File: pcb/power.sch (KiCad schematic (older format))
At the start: 25 parts, among them U16 AP22811AW5-7‎, U17 TLV62585PDRLR, U18 LP5907MFX-3.3, U4 TLV62585PDRLR

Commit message: Switch to AP3441LSHE-7B in schematic
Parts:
- removed U17, U4: TLV62585PDRLR, launch:SOT-563, symbol launch:TLV62585DRLR
- added U17, U4: AP3441LSHE-7B, launch:W-DFN2020-8_Type_C, symbol launch:AP3441LSHE-7B
- C32, C34, C35, C48, C49, C50: value 10 uF -> 22 uF
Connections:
- wire segments 58 -> 60
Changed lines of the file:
@@
 L power:GND #PWR0248
 U 1 1 5F8E3978
-P 4500 4550
-F 0 "#PWR0248" H 4500 4300 50  0001 C CNN
-F 1 "GND" H 4505 4377 50  0000 C CNN
-F 2 "" H 4500 4550 50  0001 C CNN
-F 3 "" H 4500 4550 50  0001 C CNN
-	1    4500 4550
+P 4500 4600
+F 0 "#PWR0248" H 4500 4350 50  0001 C CNN
+F 1 "GND" H 4505 4427 50  0000 C CNN
+F 2 "" H 4500 4600 50  0001 C CNN
+F 3 "" H 4500 4600 50  0001 C CNN
+	1    4500 4600
 	1    0    0    -1
 $EndComp
@@
 	1    0    0    -1
 $EndComp
-$Comp
-L launch:TLV62585DRLR U17
-U 1 1 5F8E44C6
-P 4650 4250
-F 0 "U17" H 4975 4425 50  0000 C CNN
-F 1 "TLV62585PDRLR" H 4975 4334 50  0000 C CNN
-F 2 "launch:SOT-563" H 5000 4300 50  0001 L CNN
-F 3 "${KIPRJMOD}/docs/tlv62585.pdf" V 4900 4250 50  0001 C CNN
-F 4 "Texas Instruments" H 4650 4250 50  0001 C CNN "Manufacturer"
-	1    4650 4250
-	1    0    0    -1
-$EndComp
 Wire Wire Line
 	4550 4500 4500 4500
-Wire Wire Line
-	4500 4500 4500 4550
 $Comp
 L Device:L L1
@@
 P 6400 4500
 F 0 "C34" H 6515 4546 50  0000 L CNN
-F 1 "10 uF" H 6515 4455 50  0000 L CNN
+F 1 "22 uF" H 6515 4455 50  0000 L CNN
 F 2 "Capacitor_SMD:C_0805_2012Metric" H 6438 4350 50  0001 C CNN
 F 3 "~" H 6400 4500 50  0001 C CNN
@@
 P 6850 4500
 F 0 "C35" H 6965 4546 50  0000 L CNN
-F 1 "10 uF" H 6965 4455 50  0000 L CNN
+F 1 "22 uF" H 6965 4455 50  0000 L CNN
 F 2 "Capacitor_SMD:C_0805_2012Metric" H 6888 4350 50  0001 C CNN
 F 3 "~" H 6850 4500 50  0001 C CNN
@@
 P 3950 4500
 F 0 "C32" H 4065 4546 50  0000 L CNN
-F 1 "10 uF" H 4065 4455 50  0000 L CNN
+F 1 "22 uF" H 4065 4455 50  0000 L CNN
 F 2 "Capacitor_SMD:C_0805_2012Metric" H 3988 4350 50  0001 C CNN
 F 3 "~" H 3950 4500 50  0001 C CNN
@@
 L power:GND #PWR0198
 U 1 1 604E7615
-P 4500 5600
-F 0 "#PWR0198" H 4500 5350 50  0001 C CNN
-F 1 "GND" H 4505 5427 50  0000 C CNN
-F 2 "" H 4500 5600 50  0001 C CNN
-F 3 "" H 4500 5600 50  0001 C CNN
-	1    4500 5600
-	1    0    0    -1
-$EndComp
-$Comp
-L launch:TLV62585DRLR U4
-U 1 1 604E7629
-P 4650 5300
-F 0 "U4" H 4975 5475 50  0000 C CNN
-F 1 "TLV62585PDRLR" H 4975 5384 50  0000 C CNN
-F 2 "launch:SOT-563" H 5000 5350 50  0001 L CNN
-F 3 "${KIPRJMOD}/docs/tlv62585.pdf" V 4900 5300 50  0001 C CNN
-F 4 "Texas Instruments" H 4650 5300 50  0001 C CNN "Manufacturer"
-	1    4650 5300
+P 4500 5650
+F 0 "#PWR0198" H 4500 5400 50  0001 C CNN
+F 1 "GND" H 4505 5477 50  0000 C CNN
+F 2 "" H 4500 5650 50  0001 C CNN
+F 3 "" H 4500 5650 50  0001 C CNN
+	1    4500 5650
 	1    0    0    -1
 $EndComp
 Wire Wire Line
 	4550 5550 4500 5550
-Wire Wire Line
-	4500 5550 4500 5600
 $Comp
 L Device:L L2
@@
 P 6400 5550
 F 0 "C49" H 6515 5596 50  0000 L CNN
-F 1 "10 uF" H 6515 5505 50  0000 L CNN
+F 1 "22 uF" H 6515 5505 50  0000 L CNN
 F 2 "Capacitor_SMD:C_0805_2012Metric" H 6438 5400 50  0001 C CNN
 F 3 "~" H 6400 5550 50  0001 C CNN
@@
 P 6850 5550
 F 0 "C50" H 6965 5596 50  0000 L CNN
-F 1 "10 uF" H 6965 5505 50  0000 L CNN
+F 1 "22 uF" H 6965 5505 50  0000 L CNN
 F 2 "Capacitor_SMD:C_0805_2012Metric" H 6888 5400 50  0001 C CNN
 F 3 "~" H 6850 5550 50  0001 C CNN
@@
 P 3950 5550
 F 0 "C48" H 4065 5596 50  0000 L CNN
-F 1 "10 uF" H 4065 5505 50  0000 L CNN
+F 1 "22 uF" H 4065 5505 50  0000 L CNN
 F 2 "Capacitor_SMD:C_0805_2012Metric" H 3988 5400 50  0001 C CNN
 F 3 "~" H 3950 5550 50  0001 C CNN
@@
 Text Notes 2800 3900 0    50   ~ 0
 This electronic circuit breaker\nprovides a soft start of the\ncapitive load for USB specification compliance.
+$Comp
+L launch:AP3441LSHE-7B U17
+U 1 1 60A97C2A
+P 4650 4250
+F 0 "U17" H 4975 4425 50  0000 C CNN
+F 1 "AP3441LSHE-7B" H 4975 4334 50  0000 C CNN
+F 2 "launch:W-DFN2020-8_Type_C" H 4650 4300 50  0001 L CNN
+F 3 "${KIPRJMOD}/docs/AP3441-L.pdf" V 4900 4250 50  0001 C CNN
+	1    4650 4250
+	1    0    0    -1
+$EndComp
+$Comp
+L launch:AP3441LSHE-7B U4
+U 1 1 60A990E4
+P 4650 5300
+F 0 "U4" H 4975 5475 50  0000 C CNN
+F 1 "AP3441LSHE-7B" H 4975 5384 50  0000 C CNN
+F 2 "launch:W-DFN2020-8_Type_C" H 4650 5350 50  0001 L CNN
+F 3 "${KIPRJMOD}/docs/AP3441-L.pdf" V 4900 5300 50  0001 C CNN
+	1    4650 5300
+	1    0    0    -1
+$EndComp
+Wire Wire Line
+	4550 4600 4500 4600
+Wire Wire Line
+	4500 4500 4500 4600
+Connection ~ 4500 4600
+Wire Wire Line
+	4500 5550 4500 5650
+Wire Wire Line
+	4550 5650 4500 5650
+Connection ~ 4500 5650
+$Comp
+L power:GND #PWR?
+U 1 1 60AA4E22
+P 5400 4600
+F 0 "#PWR?" H 5400 4350 50  0001 C CNN
+F 1 "GND" H 5405 4427 50  0000 C CNN
+F 2 "" H 5400 4600 50  0001 C CNN
+F 3 "" H 5400 4600 50  0001 C CNN
+	1    5400 4600
+	1    0    0    -1
+$EndComp
+$Comp
+L power:GND #PWR?
+U 1 1 60AA63CF
+P 5400 5650
+F 0 "#PWR?" H 5400 5400 50  0001 C CNN
+F 1 "GND" H 5405 5477 50  0000 C CNN
+F 2 "" H 5400 5650 50  0001 C CNN
+F 3 "" H 5400 5650 50  0001 C CNN
+	1    5400 5650
+	1    0    0    -1
+$EndComp
 $EndSCHEMATC

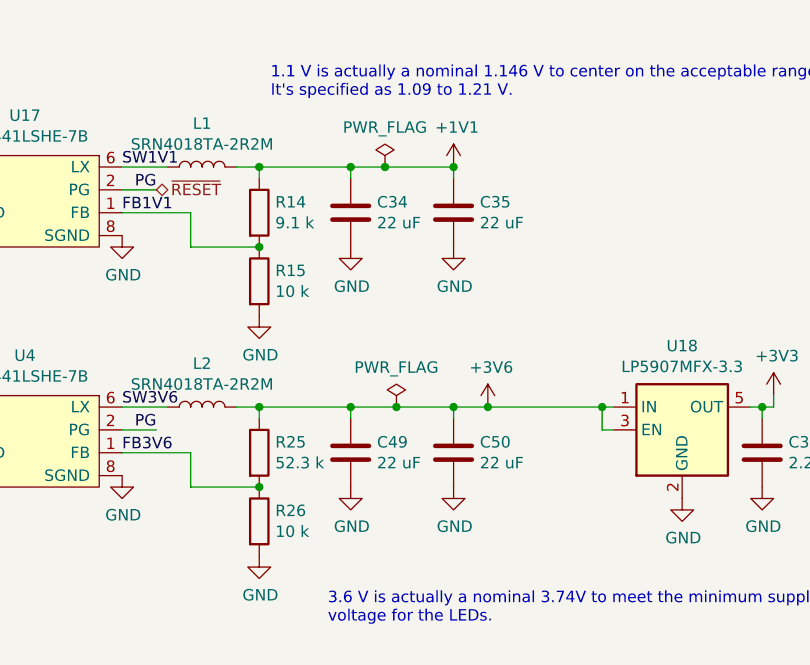
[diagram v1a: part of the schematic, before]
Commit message: Add 22pF capacitors to AP3441-L as recommended
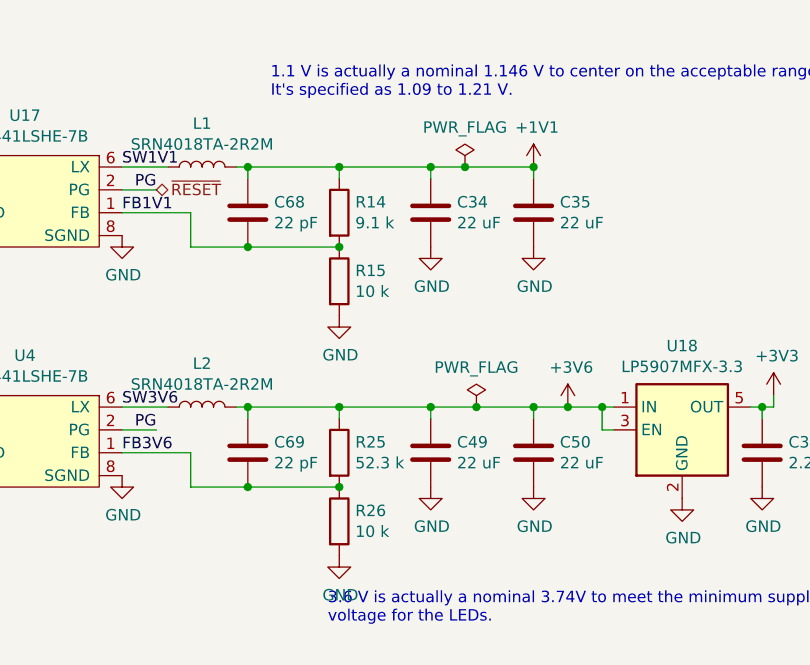
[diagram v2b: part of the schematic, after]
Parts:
- added C68, C69: 22 pF, Capacitor_SMD:C_0402_1005Metric, symbol Device:C
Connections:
- net +1V1: now also C68.1
- net +3V6: now also C69.1
- net FB1V1: now also C68.2
- net FB3V6: now also C69.2
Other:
- moved on the sheet: C34, C35, C49, C50, R14, R15, R25, R26

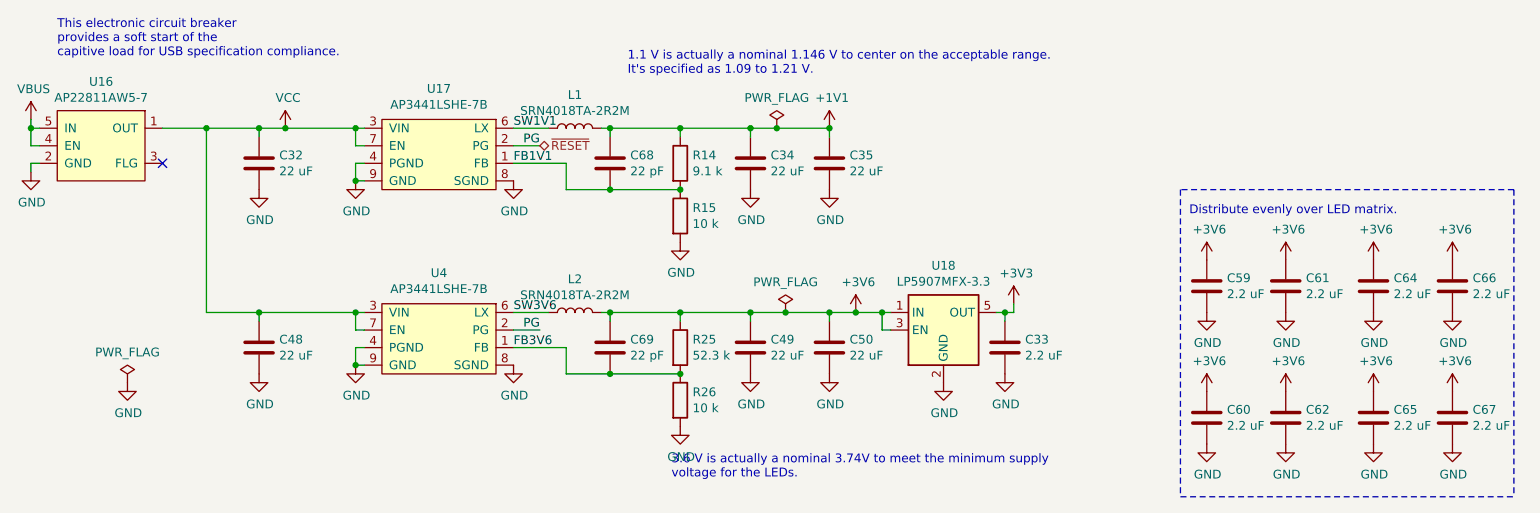
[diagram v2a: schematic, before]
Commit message: Use AP61302 for regulating 1V1 and 3V6 power planes
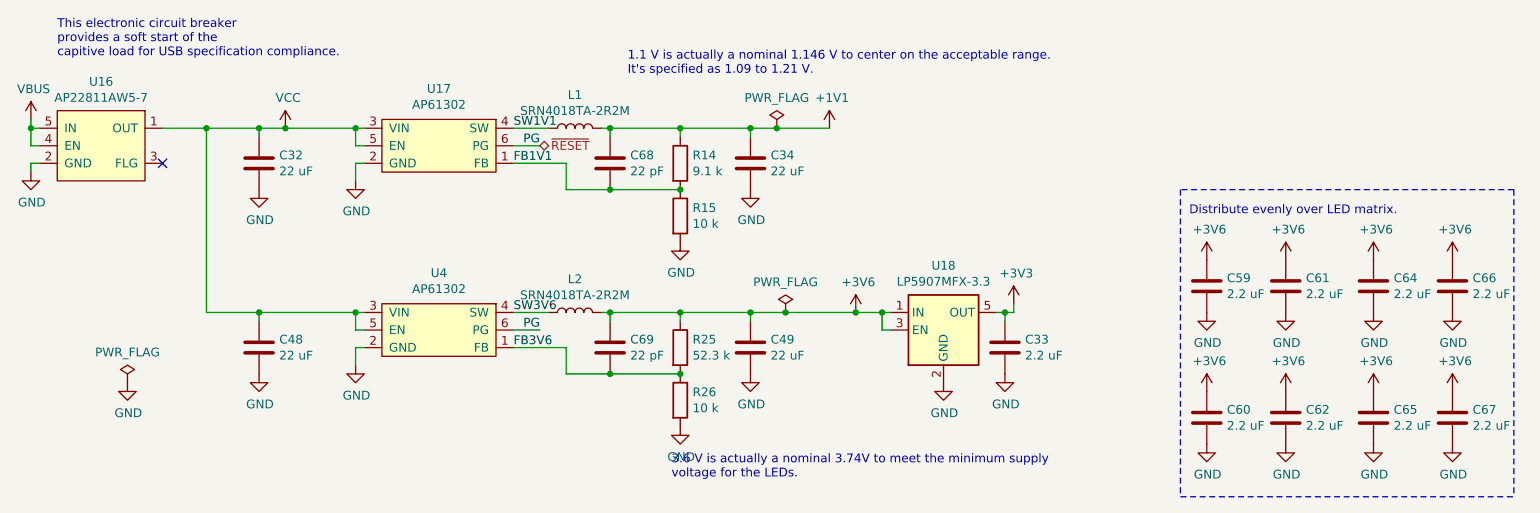
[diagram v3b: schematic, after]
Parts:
- removed C35, C50: 22 uF, Capacitor_SMD:C_0805_2012Metric, symbol Device:C
- removed U17, U4: AP3441LSHE-7B, launch:W-DFN2020-8_Type_C, symbol launch:AP3441LSHE-7B
- added U17, U4: AP61302, launch:SOT-563, symbol launch:AP61302
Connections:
- net FB1V1: now also U17.1 (FB)
- net FB3V6: now also U4.1 (FB)
- net GND: now also U17.2 (GND), U4.2 (GND)
- net SW1V1: now also U17.4 (SW)
- net SW3V6: now also U4.4 (SW)
- net VCC: now also U17.3 (VIN), U17.5 (EN), U4.3 (VIN), U4.5 (EN)
- net ~RESET: now also U17.6 (PG), U4.6 (PG)

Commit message: minor layout adjustments, feedforward cap value Change feedforward cap to 330 pF so the transfer function of the feedback   network will be similar to that of the datasheet example. Our feedback   resistors are lower and the impedance of the cap needs to be proportionally   lower.
Correct typo in notes on power schematic page.

Change buck feedforward cap footprint from Kicad lib to launch lib for consistency.

Arrange schematic components so "330 pF" does not overlap adjacent components.

Move "U4" silkscreen to not overlap inductor pad.

Add a 2nd via to each buck converter ground, move feedback components to allow.

Reroute some signal traces to reduce number of vias, have more solid ground
  planes around the buck converters. This included CL_SEL, RESET, VCC (to enable).
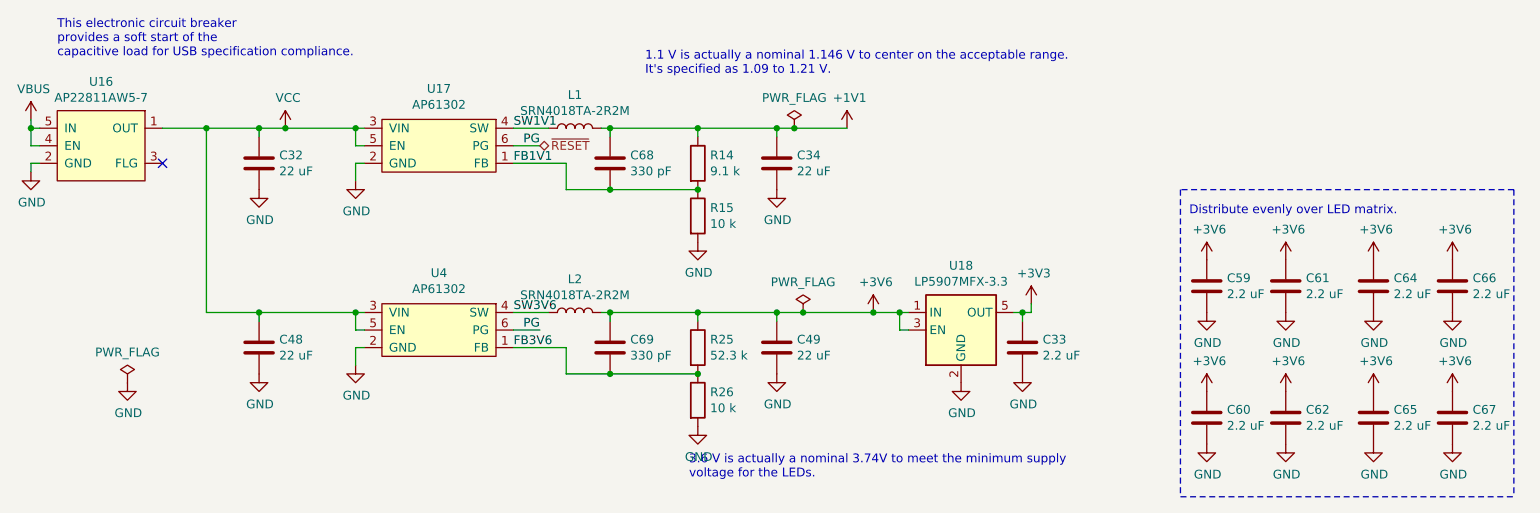
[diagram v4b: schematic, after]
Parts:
- C68, C69: value 22 pF -> 330 pF; footprint Capacitor_SMD:C_0402_1005Metric -> launch:C_0402_1005Metric
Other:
- note added: "This electronic circuit breaker\nprovides a soft start of the\ncapacitive load for USB specification compliance."
- note removed: "This electronic circuit breaker\nprovides a soft start of the\ncapitive load for USB specification compliance."
- moved on the sheet: C33, C34, C49, R14, R15, R25, R26, U18
